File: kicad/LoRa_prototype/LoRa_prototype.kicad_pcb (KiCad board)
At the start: 4 copper layers, 136 parts, among them J1 Conn_ST_STDC14, J10 SYS, J11 BME, J12 GPS, J14 SPI_FLASH, J15 SYS, J18 MCO, J2 USB_C_Receptacle_PowerOnly_6P, J3 BAT, J4 SMA Female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

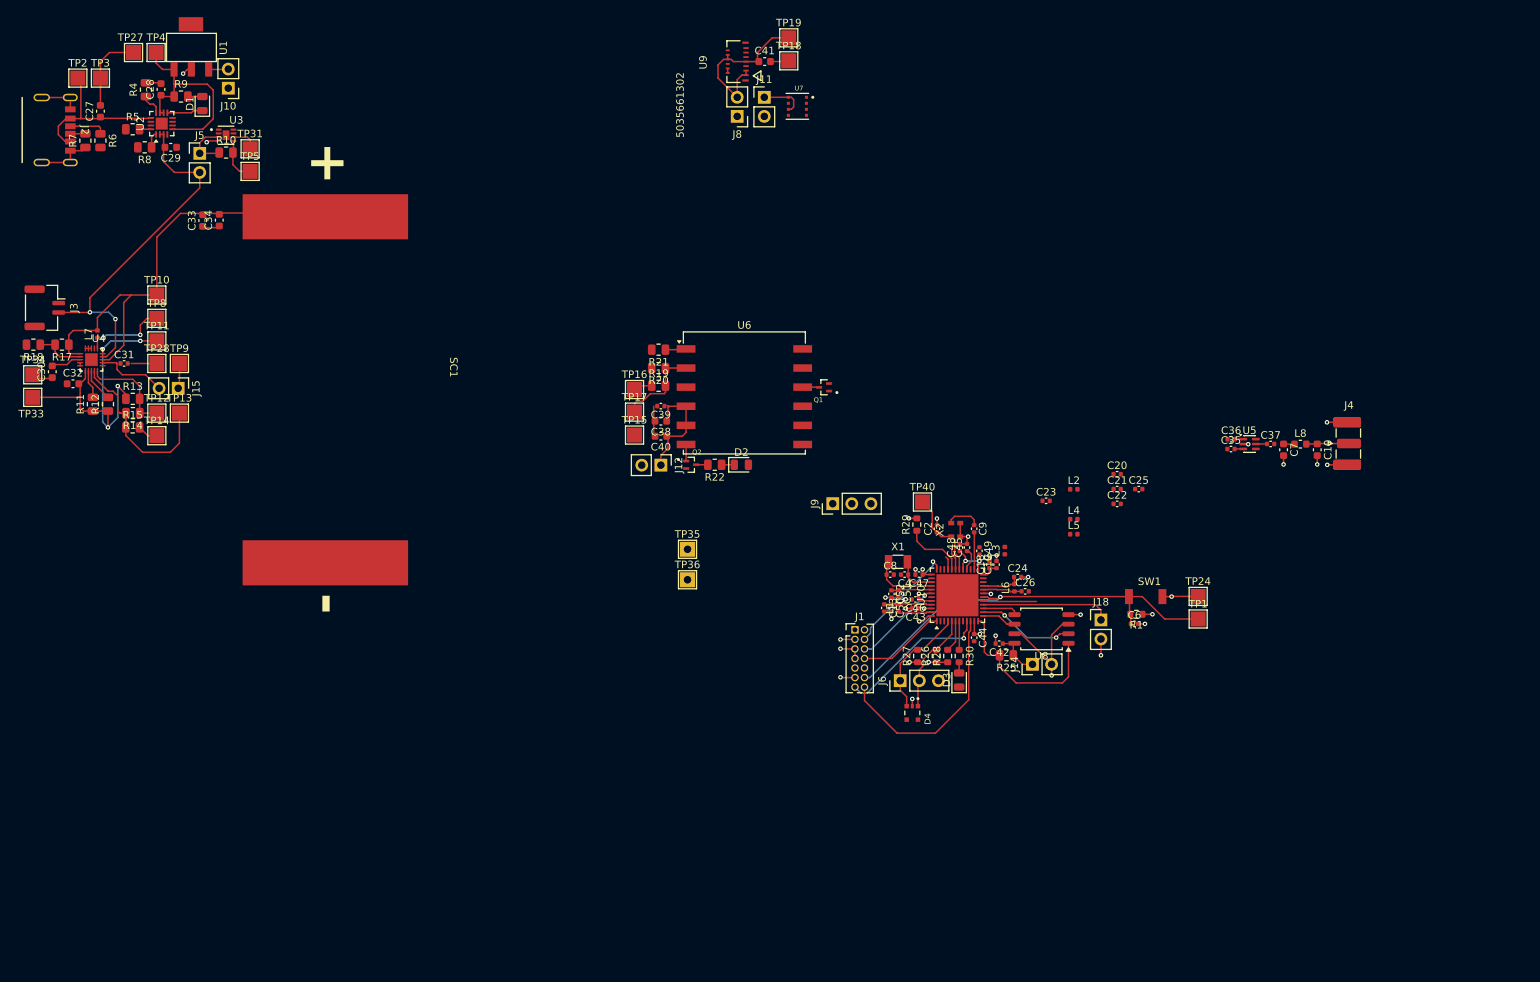
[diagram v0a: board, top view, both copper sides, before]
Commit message: Added KiNotes to project
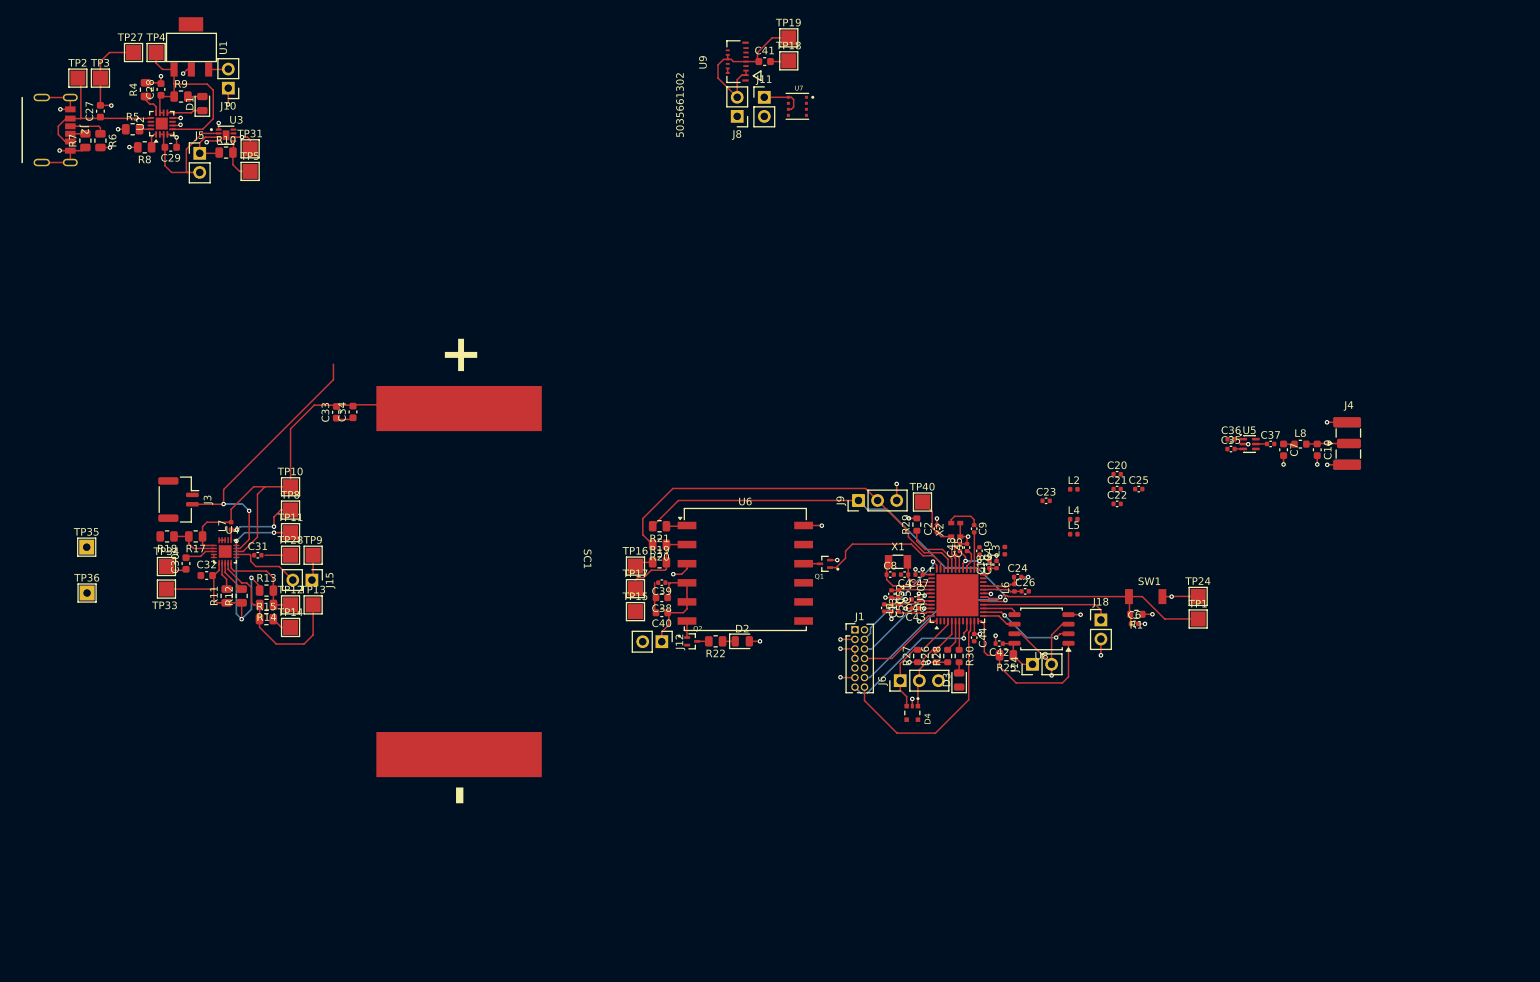
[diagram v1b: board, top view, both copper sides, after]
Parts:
- moved TP35 79.9 mm to (33.8, 99.3)
- moved TP36 79.8 mm to (33.8, 105.5)
- moved C30 31.1 mm to (47.0, 101.5)
- moved J3 31.1 mm to (46.0, 93.0)
- moved L7 31.1 mm to (53.0, 96.5)
- moved R11 31.1 mm to (52.4, 105.8)
- moved R12 31.1 mm to (54.4, 105.8)
- moved R14 31.1 mm to (57.7, 107.0)
- moved TP12 31.1 mm to (60.9, 107.0)
- moved TP13 31.1 mm to (63.9, 107.0)
- moved TP14 31.1 mm to (60.9, 110.0)
- moved C32 31.1 mm to (49.7, 103.1)
- moved J15 31.1 mm to (63.7, 103.7)
- moved R17 31.1 mm to (48.3, 97.9)
- moved SC1 31.1 mm to (83.3, 100.9)
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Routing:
- net /MCU/RX1: track 1.78 -> 51.9 mm
- net /MCU/TX1: track 7.10 -> 57.2 mm, vias 0 -> 1
- net GND: track 97.0 -> 119.8 mm, vias 28 -> 44
- net /GPS AND GAS SENSORS/GPS_RESET: track 0.00 -> 18.4 mm
- net /POWER/BAT+: track 48.1 -> 56.6 mm
- net VDD: track 41.9 -> 45.5 mm, vias 9 -> 11

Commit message: Stable commit
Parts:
- moved C28 74.5 mm to (107.6, 76.7)
- moved D1 74.5 mm to (113.1, 78.6)
- moved J10 74.5 mm to (116.5, 76.5)
- moved R6 74.5 mm to (99.5, 83.5)
- moved R7 74.5 mm to (97.5, 83.5)
- moved TP2 74.5 mm to (96.5, 75.2)
- moved TP3 74.5 mm to (99.5, 75.2)
- moved C27 74.5 mm to (99.5, 79.6)
- moved C29 74.5 mm to (108.9, 84.4)
- moved J2 74.5 mm to (95.5, 82.1)
- moved J5 74.5 mm to (112.7, 85.2)
- moved R10 74.5 mm to (116.2, 85.1)
- moved R4 74.5 mm to (105.6, 76.7)
- moved R5 74.5 mm to (103.8, 82.0)
- moved R8 74.5 mm to (105.4, 84.4)
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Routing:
- net GND: track 119.8 -> 140.9 mm, vias 44 -> 52
- net /MCU/NRST: track 56.3 -> 36.4 mm
- net /MCU_SCL1: track 15.0 -> 30.3 mm, vias 0 -> 2
- net /POWER/MPP: track 61.1 -> 68.9 mm, vias 0 -> 2
- net /POWER/BAT+: track 56.6 -> 50.8 mm
- net /MCU/RFO_LP: track 0.00 -> 4.68 mm
- net Net-(C20-Pad1): track 0.00 -> 4.28 mm
- net /MCU_SDA1: track 13.8 -> 17.9 mm, vias 0 -> 1
- net /MCU/VR_PA: track 2.45 -> 6.35 mm
- net /GPS AND GAS SENSORS/GPS_RESET: track 18.4 -> 14.9 mm
- net /MCU/RX1: track 51.9 -> 48.7 mm, vias 0 -> 2
- net Net-(C21-Pad2): track 0.00 -> 3.17 mm
- net /MCU/VCP_RX: track 29.8 -> 27.3 mm
- net VDD: track 45.5 -> 47.7 mm, vias 11 -> 13
- net /MCU/TX1: track 57.2 -> 58.6 mm, vias 1 -> 4
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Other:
- board outline added: 100 x 80 mm

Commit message: 90% done (before ground and power pour)
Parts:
- added TP6: ~{BATT_CONN}, TestPoint:TestPoint_Pad_2.0x2.0mm, F.Cu at (99.3, 113.7)
- added TP7: ~{BATT_CHG}, TestPoint:TestPoint_Pad_2.0x2.0mm, F.Cu at (99.3, 117.7)
- moved C41 111.1 mm to (163.5, 138.6), turned to -90 degrees
- moved U9 110.0 mm to (161.1, 136.9), turned to -90 degrees
- moved TP18 108.9 mm to (157.9, 139.2), turned to -90 degrees
- moved TP19 107.6 mm to (158.0, 134.8), turned to -90 degrees
- moved J8 107.6 mm to (158.1, 142.8), turned to 90 degrees
- moved J11 77.6 mm to (123.9, 117.1)
- moved U7 77.6 mm to (128.3, 118.3)
- moved C6 23.6 mm to (154.7, 123.7)
- moved SW1 23.6 mm to (156.2, 120.0)
- moved TP1 23.6 mm to (163.2, 123.0)
- moved TP24 23.6 mm to (163.2, 120.0)
- moved R1 23.6 mm to (155.0, 122.4)
- moved R29 17.9 mm to (148.2, 113.8), turned to -90 degrees
- moved R28 17.9 mm to (144.1, 96.4), turned to -90 degrees
- moved C38 1.82 mm to (151.8, 82.8)
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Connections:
- C35 pad 1: /ANTENNA/LORA_RX -> /ANTENNA/LORA_TX
- C36 pad 1: /ANTENNA/LORA_TX -> /ANTENNA/LORA_RX
- R28 pad 2: /ANTENNA/RF_SW_V2 -> /ANTENNA/RF_SW_V1
- R29 pad 1: /ANTENNA/RF_SW_V1 -> /ANTENNA/RF_SW_V2
- U10 pad 2: /POWER/~{BATT_CONN} -> unconnected-(U10-PB4-Pad2)
- U10 pad 3: /POWER/~{BATT_CHG} -> unconnected-(U10-PB5-Pad3)
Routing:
- net /MCU_SDA1: track 17.9 -> 129.7 mm, vias 1 -> 5
- net /MCU_SCL1: track 30.3 -> 129.1 mm, vias 2 -> 3
- net /GPS AND GAS SENSORS/GPS_RESET: track 14.9 -> 58.6 mm, vias 0 -> 2
- net /ANTENNA/RF_SW_V2: track 4.25 -> 46.3 mm, vias 0 -> 2
- net /ANTENNA/RF_SW_V1: track 8.41 -> 47.7 mm, vias 0 -> 2
- net /MCU/~{ALRT}: track 9.11 -> 42.8 mm, vias 0 -> 2
- net /MCU/TX1: track 58.6 -> 76.9 mm, vias 4 -> 5
- net /MCU/VFBSMPS: track 13.1 -> 28.7 mm, vias 2 -> 3
- net /POWER/~{BATT_CHG}: track 3.75 -> 18.4 mm, vias 0 -> 2
- net /MCU/NRST: track 36.4 -> 50.5 mm, vias 1 -> 2
- net /MCU/RX1: track 48.7 -> 62.7 mm
- net /ANTENNA/LORA_TX: track 0.00 -> 11.6 mm
- net /POWER/~{BATT_CONN}: track 4.41 -> 15.4 mm, vias 0 -> 2
- net GND: track 140.9 -> 149.1 mm, vias 52 -> 60
- net Net-(J8-Pin_2): track 22.2 -> 15.4 mm
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
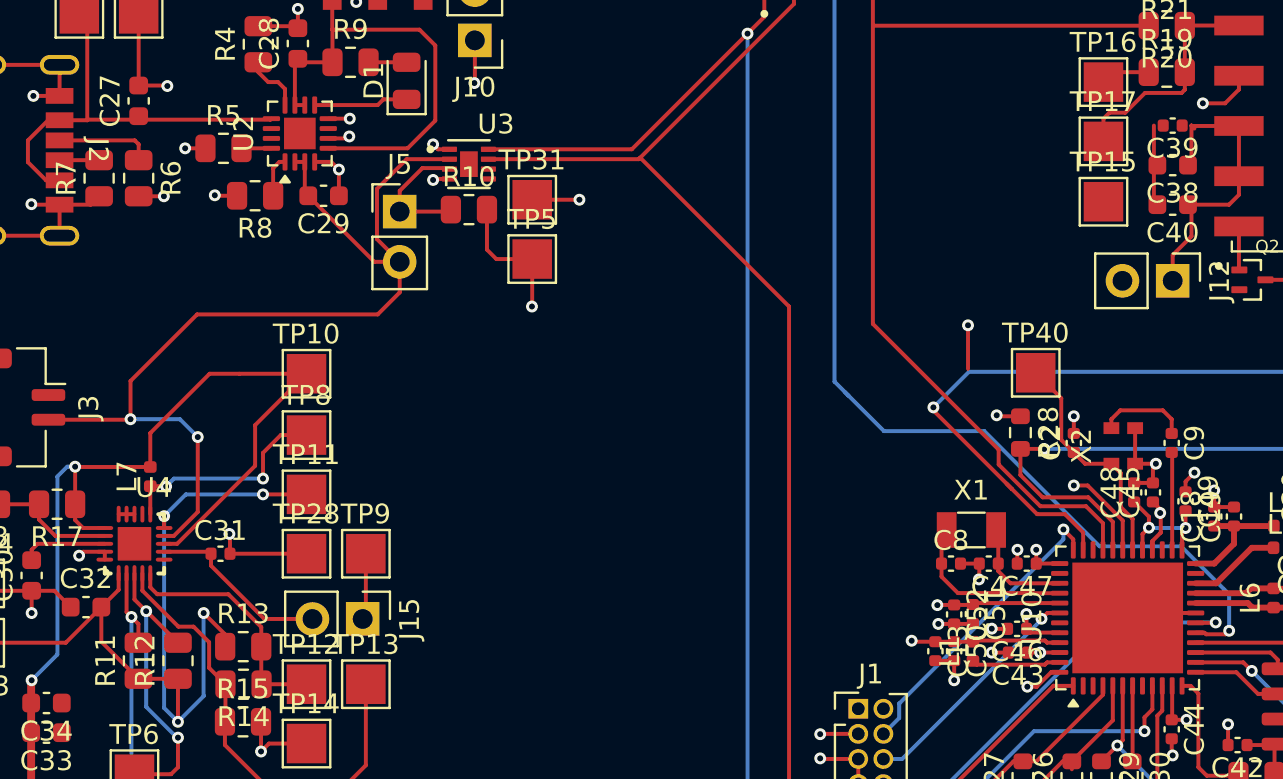
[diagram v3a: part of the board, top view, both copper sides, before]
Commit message: Added thermal vias to all ICs
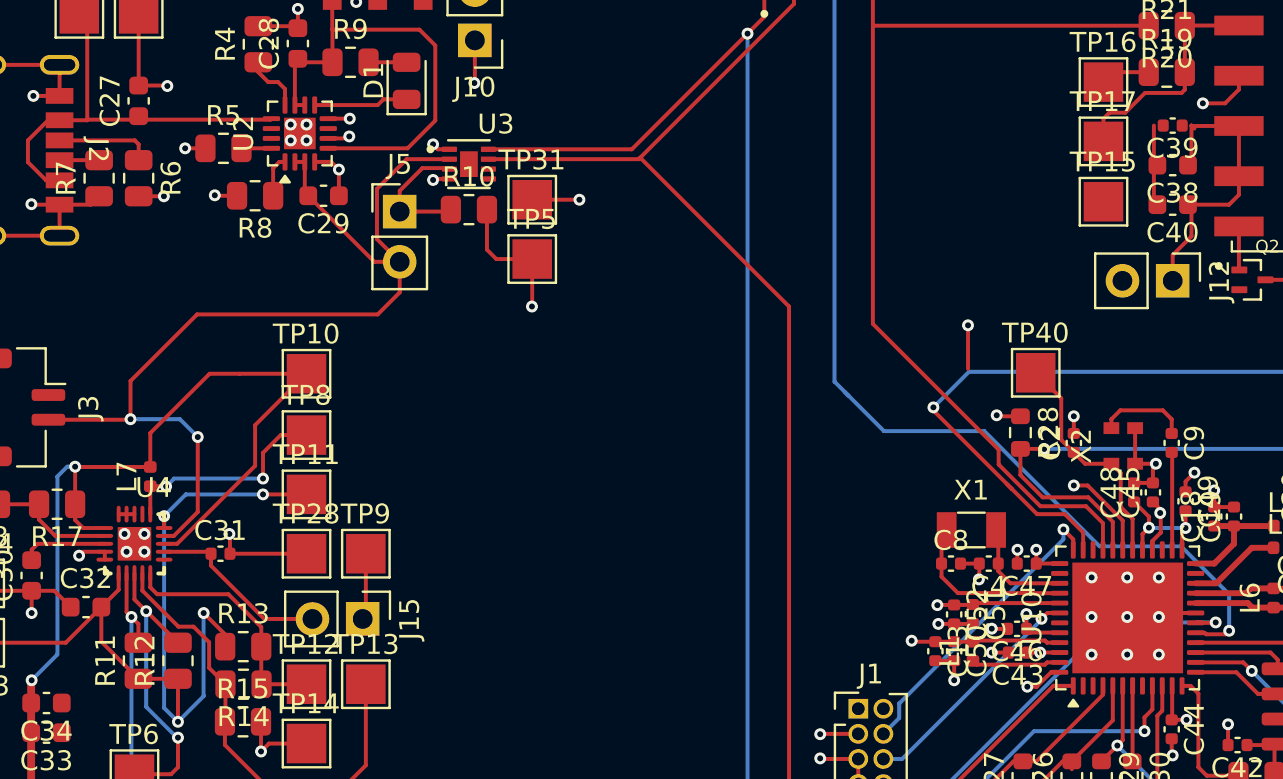
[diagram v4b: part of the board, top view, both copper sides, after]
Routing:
- net GND: track 149.1 -> 148.8 mm, vias 60 -> 77

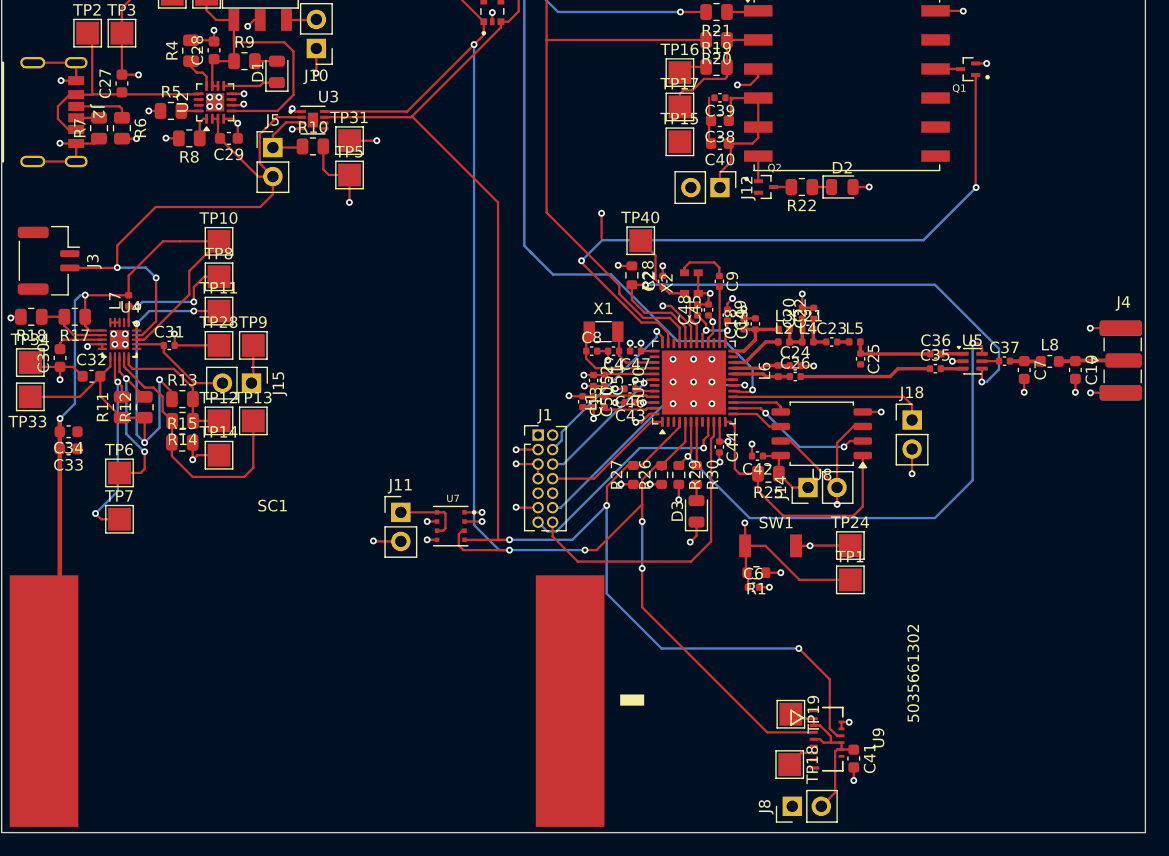
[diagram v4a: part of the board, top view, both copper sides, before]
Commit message: Connected all items (with 56 DRC violations)
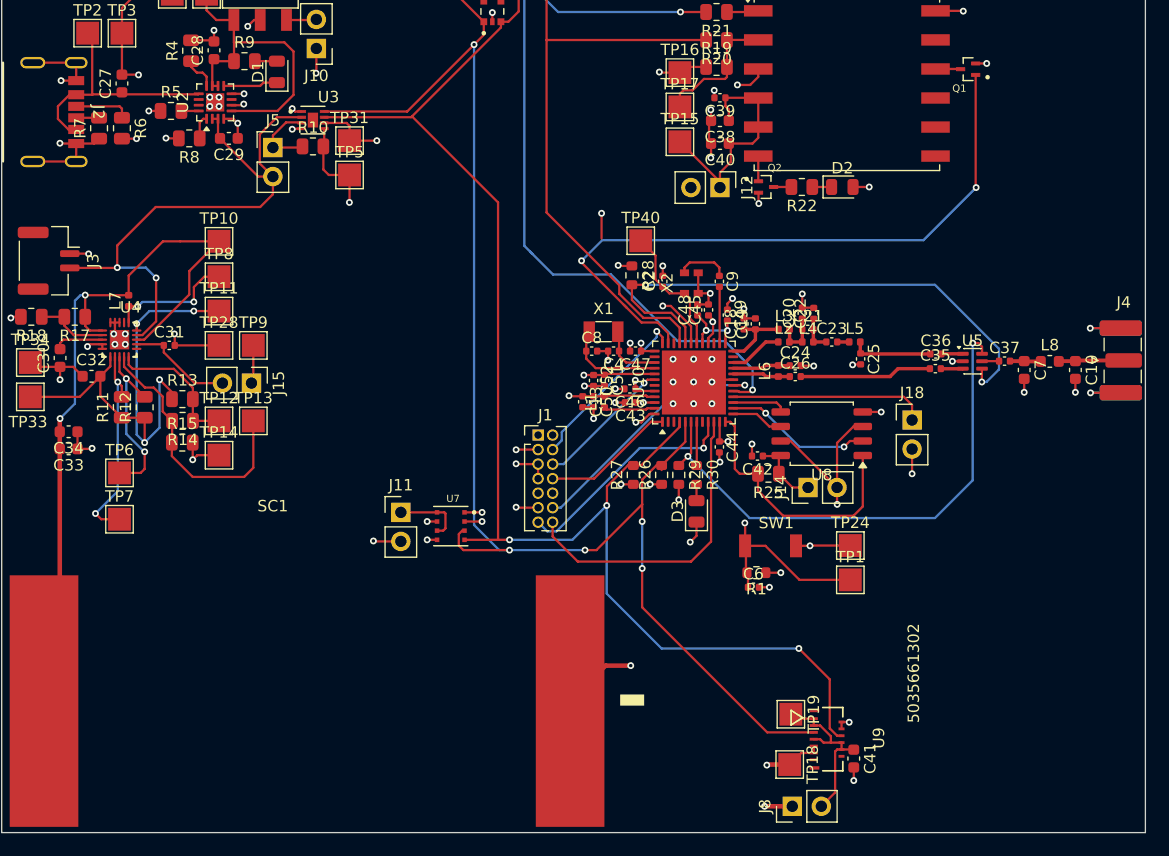
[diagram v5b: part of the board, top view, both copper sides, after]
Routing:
- net GND: track 148.8 -> 176.8 mm, vias 77 -> 87
- net Net-(J12-Pin_1): track 15.0 -> 20.8 mm
- net VDD: track 52.2 -> 54.6 mm, vias 17 -> 18
- net /MCU/~{ALRT}: track 42.8 -> 44.3 mm
- added copper zone on In1.Cu, net GND
- added copper zone on In2.Cu, net VDD

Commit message: Stable commit (only 11 DRC violations now)
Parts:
- moved SC1 7.80 mm to (115.7, 140.8)
- moved J4 0.30 mm to (186.8, 103.8)
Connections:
- U2 pad 17: (no net) -> GND
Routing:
- net GND: track 176.8 -> 170.2 mm, vias 87 -> 86
- net /POWER/MPP: track 70.0 -> 75.5 mm
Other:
- board size 100 x 80 mm -> 100 x 90 mm

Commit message: Stable commit (0 DRC violations 267 warnings)
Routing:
- net GND: track 170.2 -> 178.5 mm, vias 86 -> 88
